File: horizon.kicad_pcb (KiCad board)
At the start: 2 copper layers, 218 parts, among them J10 Conn_01x02_Pin, J11 USB_C_Receptacle_USB2.0_16P, J13 1x3 servo, J14 1x3 servo, J6 1x3 servo, J9 1x3 servo, Q1 2N7002, Q10 2N7002, Q11 2N7002, Q12 2N7002, Q13 2N7002, Q2 DMG2301L, Q3 2N7002, Q4 2N7002, Q5 2N7002, Q6 2N7002, Q7 BSS138, U10 LSM6DS3, U12 TPS63061, U13 LTC4412xS6, U14 TPS61092, U15 AP2112K-3.3, U16 TPS61092, U3 NMCU, U4 TMCU, U5 LPS22HB, U7 SX1276, U8 NAND, U9 TPS82130

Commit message: Added GPS footprint
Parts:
- added U6: GPS, RF_GPS:Quectel_L96, F.Cu at (219.2, 99.5)

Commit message: schematic(not much)
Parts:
- removed C11, C9: C, Capacitor_SMD:C_0603_1608Metric
- removed C12, C13: C, Capacitor_SMD:C_0201_0603Metric
- removed C37: 10u, Capacitor_SMD:C_0201_0603Metric
- removed C38: 2u2, Capacitor_SMD:C_0201_0603Metric
- removed C39: 100u, Capacitor_SMD:C_0201_0603Metric
- removed C40, C41, C42, C43: 10uF, Capacitor_SMD:C_0201_0603Metric
- removed D24, D25: PMEG6020ER, Diode_SMD:Nexperia_CFP3_SOD-123W
- removed L3, L4: SLF7055T-6R8N2R8-3PF, Inductor_SMD:L_7.3x7.3_H4.5
- removed Q12, Q13: 2N7002, Package_TO_SOT_SMD:SOT-23
- removed R1: 90k, Resistor_SMD:R_0603_1608Metric
- removed R2: 10k, Resistor_SMD:R_0603_1608Metric
- removed R48, R49, R51: 100k, Resistor_SMD:R_0603_1608Metric
- removed R50: 430k, Resistor_SMD:R_0603_1608Metric
- removed U12: TPS63061, Package_SON:Texas_S-PWSON-N10_ThermalVias
- removed U16: TPS61092, Package_DFN_QFN:Texas_RSA_VQFN-16-1EP_4x4mm_P0.65mm_EP2.7x2.7mm_ThermalVias
- added D23: PMEG6020ER, Diode_SMD:Nexperia_CFP3_SOD-123W, F.Cu at (91.6, -19.6)
- added IC1: A3909, A3909:MSOP10-PAD, B.Cu at (326.9, -6.02)
- added J1: Micro_SD_Card_Det1, Connector_Card:microSD_HC_Hirose_DM3D-SF, B.Cu at (314.4, -47.6)
- added J12: Conn_01x04, Connector_PinSocket_2.54mm:PinSocket_1x04_P2.54mm_Vertical, F.Cu at (287.8, -3.10)
- added J15: arming terminal, TerminalBlock_Phoenix:TerminalBlock_Phoenix_MKDS-1,5-2-5.08_1x02_P5.08mm_Horizontal, F.Cu at (232.4, -34.0)
- added J16: arming terminal, TerminalBlock_Phoenix:TerminalBlock_Phoenix_MKDS-1,5-2-5.08_1x02_P5.08mm_Horizontal, F.Cu at (232.4, -21.9)
- added J17: arming terminal, TerminalBlock_Phoenix:TerminalBlock_Phoenix_MKDS-1,5-2-5.08_1x02_P5.08mm_Horizontal, F.Cu at (244.6, -46.1)
- added J18: arming terminal, TerminalBlock_Phoenix:TerminalBlock_Phoenix_MKDS-1,5-2-5.08_1x02_P5.08mm_Horizontal, F.Cu at (244.6, -34.0)
- added J19: Screw_Terminal_01x02, TerminalBlock_Phoenix:TerminalBlock_Phoenix_MKDS-1,5-2-5.08_1x02_P5.08mm_Horizontal, F.Cu at (244.6, -21.9)
- added J2: Conn_02x03_Counter_Clockwise, Connector_PinSocket_2.54mm:PinSocket_2x03_P2.54mm_Vertical, F.Cu at (154.3, -34.8)
- added J20: Screw_Terminal_01x02, TerminalBlock_Phoenix:TerminalBlock_Phoenix_MKDS-1,5-2-5.08_1x02_P5.08mm_Horizontal, F.Cu at (256.8, -46.1)
- added J21: Screw_Terminal_01x02, TerminalBlock_Phoenix:TerminalBlock_Phoenix_MKDS-1,5-2-5.08_1x02_P5.08mm_Horizontal, F.Cu at (256.8, -34.0)
- added J22: Screw_Terminal_01x02, TerminalBlock_Phoenix:TerminalBlock_Phoenix_MKDS-1,5-2-5.08_1x02_P5.08mm_Horizontal, F.Cu at (256.8, -21.9)
- added J5: Screw_Term, TerminalBlock_Phoenix:TerminalBlock_Phoenix_MKDS-1,5-2-5.08_1x02_P5.08mm_Horizontal, F.Cu at (232.4, -46.1)
- added J7: Conn_02x03_Counter_Clockwise, Connector_PinSocket_2.54mm:PinSocket_2x03_P2.54mm_Vertical, F.Cu at (161.4, -34.8)
- added J8: Conn_02x03_Counter_Clockwise, Connector_PinSocket_2.54mm:PinSocket_2x03_P2.54mm_Vertical, F.Cu at (168.6, -34.8)
- added Q8: IRLML6402, Package_TO_SOT_SMD:SOT-23, F.Cu at (272.8, -27.2)
- added Q9: IRLML6402, Package_TO_SOT_SMD:SOT-23, F.Cu at (272.8, -22.6)
- added U1: MMCU, MK20DX256VLH7:QFP50P1200X1200X160-64N, B.Cu at (128.6, 86.4)
- added U2: IMU, BNO086:IC_BNO086, B.Cu at (327.1, -10.8)
- added Y1: Crystal, Crystal:Crystal_SMD_0603-2Pin_6.0x3.5mm, F.Cu at (139.0, -5.94)
- added Y2: 32.768kHz, Crystal:Crystal_SMD_0603-2Pin_6.0x3.5mm, F.Cu at (260.8, -13.5)
- C72: value 100nF -> 1uF
- FL5, J11, U10, U13, U14, U15, U3, U4, U5, U6, U7, U8, U9: moved to B.Cu
- Q1, Q10, Q11, Q3, Q4, Q5, Q6: value 2N7002 -> IRLML6402
- moved D15 196.5 mm to (278.3, -9.73)
- moved D16 196.5 mm to (278.3, -4.87)
- moved D17 196.5 mm to (278.3, 0.00)
- moved J14 181.9 mm to (291.5, -31.9)
- moved J13 181.9 mm to (286.9, -31.9)
- moved J9 181.8 mm to (282.2, -31.9)
- moved Q1 181.8 mm to (267.9, -31.8)
- moved Q3 181.8 mm to (267.9, -27.2)
- moved Q4 181.8 mm to (267.9, -22.6)
- moved Q5 181.8 mm to (267.9, -17.9)
- moved Q6 181.8 mm to (267.9, -13.3)
- moved Q7 181.8 mm to (272.8, -31.8)
- moved J6 181.8 mm to (277.6, -31.9)
- moved C14 181.8 mm to (276.5, -23.6)
- moved C15 181.8 mm to (276.5, -21.9)
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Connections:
- C32 pad 1: Net-(D20-K) -> Net-(D23-K)
- D20 pad 1: Net-(D20-K) -> +5V
- Q10 pad 2: Net-(D3-K) -> Net-(D5-K)
- Q11 pad 2: Net-(D4-K) -> Net-(D6-K)
- R58 pad 2: Net-(Q10-D) -> Net-(Q8-D)
- R59 pad 2: Net-(Q11-D) -> Net-(Q9-D)
- R60 pad 2: Net-(Q12-D) -> Net-(Q10-D)
- R61 pad 2: Net-(Q13-D) -> Net-(Q11-D)
- R78 pad 2: Net-(Q10-D) -> Net-(Q8-D)
- R79 pad 2: Net-(Q10-G) -> Net-(Q8-G)
- R80 pad 2: Net-(Q11-D) -> Net-(Q9-D)
- R81 pad 2: Net-(Q11-G) -> Net-(Q9-G)
- R82 pad 2: Net-(Q12-D) -> Net-(Q10-D)
- R83 pad 2: Net-(Q12-G) -> Net-(Q10-G)
- R84 pad 2: Net-(Q13-D) -> Net-(Q11-D)
- R85 pad 2: Net-(Q13-G) -> Net-(Q11-G)
- U9 pad 1: Net-(D20-K) -> Net-(D23-K)
- U9 pad 2: Net-(D20-K) -> Net-(D23-K)
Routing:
- net Net-(D8-I/O1): track 0.00 -> 34.9 mm, vias 0 -> 1
- net Net-(FL5-Pad4): track 0.00 -> 33.8 mm
- net Net-(FL5-Pad3): track 0.00 -> 33.8 mm
- net Net-(D8-I/O2): track 0.00 -> 20.2 mm, vias 0 -> 1
- net GND: track 0.00 -> 18.3 mm, vias 0 -> 4
- net Net-(D26-A): track 0.00 -> 13.9 mm, vias 0 -> 1
- net Net-(J11-CC1): track 0.00 -> 2.49 mm, vias 0 -> 1
- net Net-(J11-CC2): track 0.00 -> 0.67 mm, vias 0 -> 1
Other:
- board outline added: 168.3 x 97.7 mm
- copper layers 2 -> 6
- board text removed: "50x100mm"

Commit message: started pcb
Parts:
- removed FL5, FL6: Choke_CommonMode_PulseElectronics_PH9455x105NL, Inductor_THT:L_CommonMode_PulseElectronics_PH9455x105NL_1
- removed R13, R14, R15, R16, R17, R18: 22, Resistor_SMD:R_0603_1608Metric
- added C37: 4n7, Capacitor_SMD:C_0603_1608Metric, F.Cu at (103.5, 23.7)
- added C38: 100n, Capacitor_SMD:C_0603_1608Metric, F.Cu at (104.2, 26.0)
- added C39: 4n7, Capacitor_SMD:C_0603_1608Metric, F.Cu at (115.4, 23.5)
- added C40: 100n, Capacitor_SMD:C_0603_1608Metric, F.Cu at (116.3, 25.8)
- added D10: PRTR5V0U2X, Package_TO_SOT_SMD:SOT-143, F.Cu at (100.6, 27.3)
- added D11: LED, LED_SMD:LED_0603_1608Metric, F.Cu at (119.2, 26.6)
- added D12: PRTR5V0U2X, Package_TO_SOT_SMD:SOT-143, F.Cu at (113.1, 27.8)
- added D27: PMEG6020ER, Diode_SMD:Nexperia_CFP3_SOD-123W, F.Cu at (104.4, 29.4)
- added D28: PMEG6020ER, Diode_SMD:Nexperia_CFP3_SOD-123W, F.Cu at (117.3, 29.3)
- added D9: LED, LED_SMD:LED_0603_1608Metric, F.Cu at (106.7, 26.8)
- added J23: USB_C_Receptacle_USB2.0_16P, Connector_USB:USB_C_Receptacle_Amphenol_124019772112A, B.Cu at (100.8, 21.1)
- added J24: USB_C_Receptacle_USB2.0_16P, Connector_USB:USB_C_Receptacle_Amphenol_124019772112A, B.Cu at (113.0, 21.2)
- added R48: 5k1, Resistor_SMD:R_0603_1608Metric, F.Cu at (98.9, 23.6)
- added R49: 5k1, Resistor_SMD:R_0603_1608Metric, F.Cu at (103.1, 21.5)
- added R50: 330, Resistor_SMD:R_0603_1608Metric, F.Cu at (104.4, 27.5)
- added R86: 5k1, Resistor_SMD:R_0603_1608Metric, F.Cu at (110.9, 24.2)
- added R96: 5k1, Resistor_SMD:R_0603_1608Metric, F.Cu at (115.3, 21.2)
- added R97: 330, Resistor_SMD:R_0603_1608Metric, F.Cu at (116.9, 27.4)
- added TP14: TestPoint, TestPoint:TestPoint_Pad_1.0x1.0mm, F.Cu at (97.3, 26.2)
- added TP15: TestPoint, TestPoint:TestPoint_Pad_1.0x1.0mm, F.Cu at (100.6, 30.6)
- added TP16: TestPoint, TestPoint:TestPoint_Pad_1.0x1.0mm, F.Cu at (110.3, 26.0)
- added TP17: TestPoint, TestPoint:TestPoint_Pad_1.0x1.0mm, F.Cu at (113.2, 31.2)
- C14, C15, C16, C17, C18, C19, C20, C21, C22, C23, C24, C25, C26, C27, C28, C29, C30, C31, C32, C33, C34, C35, C36, C44, C45, C46, C47, C48, C49, C50, C51, C52, C53, C54, C55, C56, C57, C58, C61, C62, C63, C64, C65, C66, C67, C68, C69, C70, C71, C72, C73, C74, C75, C76, C77, C78: footprint Capacitor_SMD:C_0201_0603Metric -> Capacitor_SMD:C_0603_1608Metric
- D7: footprint LED_SMD:LED_0201_0603Metric -> LED_SMD:LED_0603_1608Metric
- moved C29 130.7 mm to (111.2, 105.3)
- moved C30 130.7 mm to (111.2, 107.0)
- moved C31 130.7 mm to (113.7, 103.5)
- moved L2 130.7 mm to (104.0, 116.8)
- moved R40 130.7 mm to (97.3, 103.9)
- moved R41 130.7 mm to (97.3, 106.4)
- moved R42 130.7 mm to (97.3, 108.9)
- moved R43 130.7 mm to (97.3, 111.4)
- moved U14 119.8 mm to (119.4, 109.2)
- moved J10 109.8 mm to (108.3, 94.3), turned to -90 degrees
- moved J8 107.8 mm to (80.5, 27.4)
- moved U4 105.1 mm to (52.2, 45.5)
- moved U1 103.8 mm to (39.7, 33.0)
- moved U3 97.2 mm to (27.2, 45.5)
- moved J7 96.7 mm to (80.6, 18.3)
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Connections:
- D19 pad 2: usbc -> VBUS
- D8 pad 2: Net-(D8-I/O1) -> D+ MMCU
- D8 pad 3: Net-(D8-I/O2) -> D- MMCU
- J11 pad A6: Net-(D8-I/O1) -> D+ MMCU
- J11 pad A7: Net-(D8-I/O2) -> D- MMCU
- J11 pad B6: Net-(D8-I/O1) -> D+ MMCU
- J11 pad B7: Net-(D8-I/O2) -> D- MMCU
- TP12 pad 1: Net-(D8-I/O1) -> D+ MMCU
- TP13 pad 1: Net-(D8-I/O2) -> D- MMCU
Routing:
- net Net-(D8-I/O1): track 34.9 -> 0.00 mm, vias 1 -> 0
- net GND: track 18.3 -> 52.7 mm, vias 4 -> 10
- net Net-(FL5-Pad4): track 33.8 -> 0.00 mm
- net Net-(FL5-Pad3): track 33.8 -> 0.00 mm
- net Net-(D8-I/O2): track 20.2 -> 0.00 mm, vias 1 -> 0
- net Net-(D10-VCC): track 0.00 -> 18.3 mm, vias 0 -> 1
- net Net-(D12-VCC): track 0.00 -> 13.8 mm, vias 0 -> 1
- net D- DMCU-2: track 0.00 -> 11.2 mm, vias 0 -> 2
- net D- MMCU: track 0.00 -> 10.9 mm, vias 0 -> 2
- net D- DMCU-1: track 0.00 -> 10.7 mm, vias 0 -> 2
- net D+ DMCU-1: track 0.00 -> 7.29 mm, vias 0 -> 1
- net D+ DMCU-2: track 0.00 -> 7.09 mm, vias 0 -> 1
- net D+ MMCU: track 0.00 -> 6.74 mm, vias 0 -> 1
- net Net-(D26-A): track 13.9 -> 17.4 mm
- net Net-(J23-CC1): track 0.00 -> 2.68 mm, vias 0 -> 1
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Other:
- board size 168.3 x 97.7 mm -> 50 x 100 mm
- copper layers 6 -> 4

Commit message: pcb
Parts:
- IC1, J1, U1, U10, U13, U14, U15, U2, U3, U4, U5, U6, U7, U8, U9: moved to F.Cu
- J2, J7, J8: moved to B.Cu
- moved J1 219.5 mm to (227.3, 153.8), turned to 0 degrees
- moved C54 211.6 mm to (184.0, 162.9)
- moved C26 206.5 mm to (180.0, 162.9)
- moved C25 205.9 mm to (180.0, 160.4)
- moved C24 205.2 mm to (180.0, 157.9)
- moved C23 204.5 mm to (180.0, 155.4)
- moved C53 199.0 mm to (184.0, 160.4)
- moved C52 198.3 mm to (184.0, 157.9)
- moved C51 197.7 mm to (184.0, 155.4)
- moved C50 197.0 mm to (184.0, 152.9)
- moved C49 196.3 mm to (184.0, 150.4)
- moved C48 195.7 mm to (184.0, 147.8)
- moved C47 195.0 mm to (184.0, 145.3)
- moved C22 192.0 mm to (180.0, 152.9)
- moved C21 191.4 mm to (180.0, 150.4)
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
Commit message: pcb
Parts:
- D21, D22: footprint LED_SMD:LED_0201_0603Metric -> LED_SMD:LED_0603_1608Metric
- U1, U3, U4: moved to B.Cu
- moved J2 99.3 mm to (95.7, 114.1), turned to -90 degrees
- moved D21 96.5 mm to (99.6, 40.0), turned to 180 degrees
- moved J7 96.0 mm to (77.8, 114.1), turned to -90 degrees
- moved J10 94.8 mm to (121.5, 41.0), turned to 90 degrees
- moved U14 93.7 mm to (113.2, 39.3)
- moved D23 93.3 mm to (107.3, 44.6), turned to -90 degrees
- moved R42 93.1 mm to (113.0, 35.8)
- moved R41 90.5 mm to (117.5, 36.7)
- moved D20 90.4 mm to (109.6, 44.6), turned to 90 degrees
- moved D19 89.8 mm to (103.5, 41.3), turned to 180 degrees
- moved U1 89.5 mm to (100.8, 53.6), turned to 135 degrees
- moved C31 89.2 mm to (108.9, 34.7), turned to 90 degrees
- moved D22 88.6 mm to (101.7, 49.6), turned to 90 degrees
- moved U4 88.4 mm to (113.3, 66.1), turned to 135 degrees
- moved J8 87.6 mm to (86.7, 114.1), turned to -90 degrees
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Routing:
- net +3.3V: track 0.00 -> 53.8 mm, vias 0 -> 1
- net VBUS: track 0.00 -> 52.5 mm
- net D+ MMCU: track 6.74 -> 49.7 mm, vias 1 -> 2
- net D+ DMCU-1: track 7.29 -> 48.9 mm, vias 1 -> 2
- net D- DMCU-1: track 10.7 -> 50.8 mm, vias 2 -> 3
- net GND: track 52.7 -> 90.5 mm, vias 10 -> 33
- net D- MMCU: track 10.9 -> 47.5 mm, vias 2 -> 3
- net D+ DMCU-2: track 7.09 -> 43.2 mm, vias 1 -> 2
- net D- DMCU-2: track 11.2 -> 45.3 mm, vias 2 -> 3
- net Net-(U15-EN): track 0.00 -> 17.3 mm
- net Net-(J10-Pin_1): track 0.00 -> 17.3 mm
- net bat: track 0.00 -> 14.2 mm
- net POWAAAA: track 0.00 -> 10.9 mm
- net Net-(L2-Pad2): track 0.00 -> 6.47 mm
- net Net-(U9-FB): track 0.00 -> 6.00 mm
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
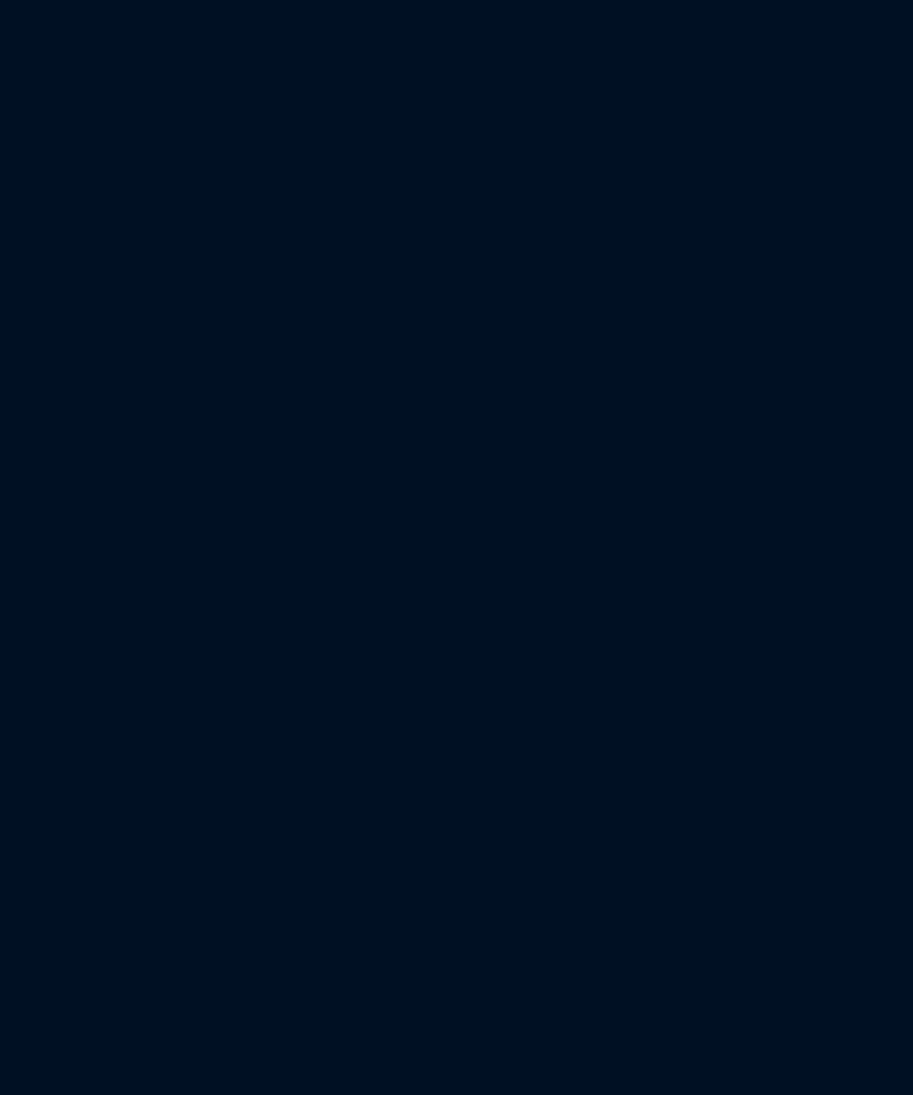
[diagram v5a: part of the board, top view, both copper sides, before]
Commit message: Hopefully added BL, and all the remaining footprints
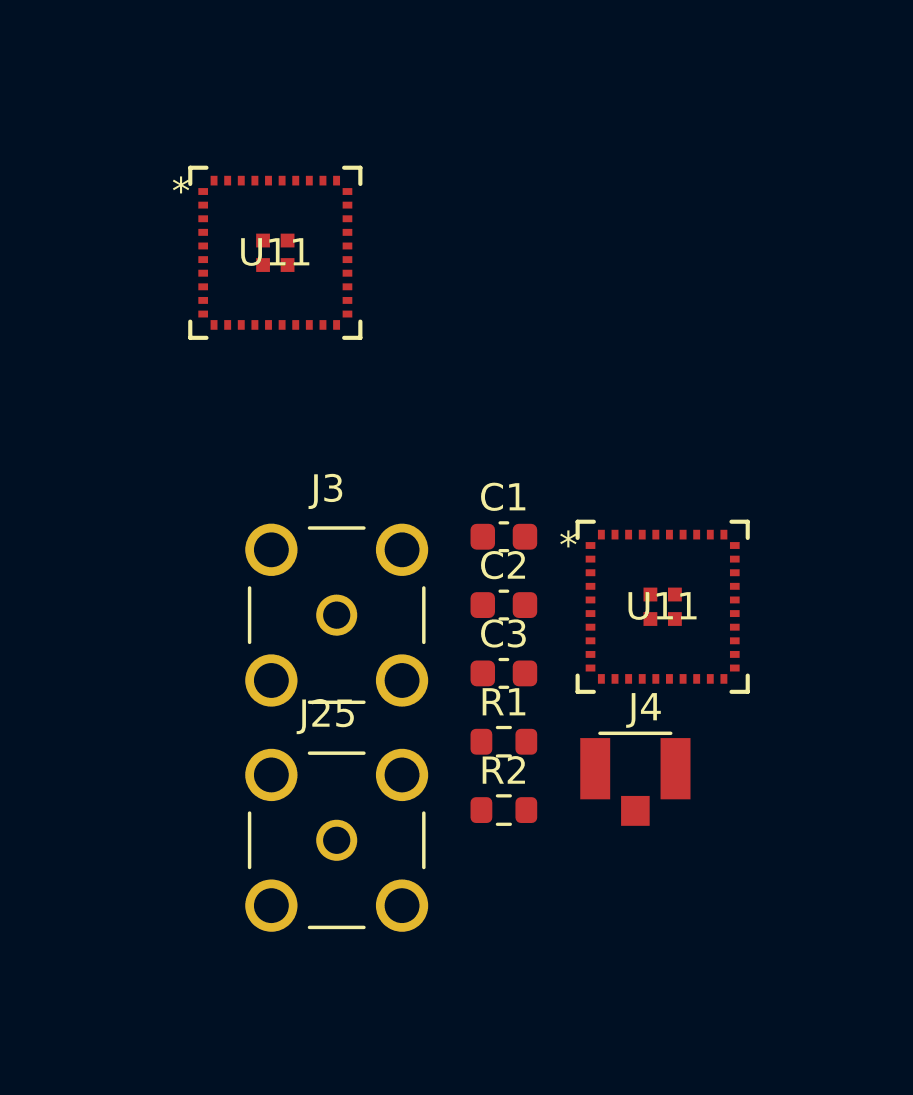
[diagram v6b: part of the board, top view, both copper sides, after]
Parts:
- added C1: 100 nF, Capacitor_SMD:C_0603_1608Metric, F.Cu at (149.5, 51.3)
- added C2: 100 nF, Capacitor_SMD:C_0603_1608Metric, F.Cu at (149.5, 53.8)
- added C3: 100 nF, Capacitor_SMD:C_0603_1608Metric, F.Cu at (149.5, 56.4)
- added J25: Conn_Coaxial, SMA:LPRS_SMA_CONNECTOR, F.Cu at (143.4, 62.5)
- added J3: Conn_Coaxial, SMA:LPRS_SMA_CONNECTOR, F.Cu at (143.4, 54.2)
- added J4: H9161TR-ND, U.FL:HRS_U.FL-R-SMT_01_, F.Cu at (154.3, 59.9)
- added R1: 10 kΩ, Resistor_SMD:R_0603_1608Metric, F.Cu at (149.5, 58.9)
- added R2: 10 kΩ, Resistor_SMD:R_0603_1608Metric, F.Cu at (149.5, 61.4)
- added U11: BGM220SC12WGA2R, BGM220SC12WGA2R:BGM220SC12WGA2R, F.Cu at (141.1, 40.9)
- added U11: BGM220SC12WGA2R, BGM220S_SIL:BGM220SC12WGA2R, F.Cu at (155.3, 53.9)
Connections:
- U3 pad 19: unconnected-(U3-PA10-Pad19) -> BGM_RESET
- U3 pad 51: unconnected-(U3-PA27-Pad51) -> BGM_CS
- U3 pad 53: unconnected-(U3-PA28-Pad53) -> BGM_INT
